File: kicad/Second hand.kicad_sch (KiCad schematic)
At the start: 74 parts, among them Q201 DMN32D2, Q210 DMP2900, Q223 DMN32D2, Q232 DMP2900, Q245 DMN32D2, Q254 DMP2900, Q267 DMN32D2, Q289 DMN32D2, U201 74HC595, U202 74HC595

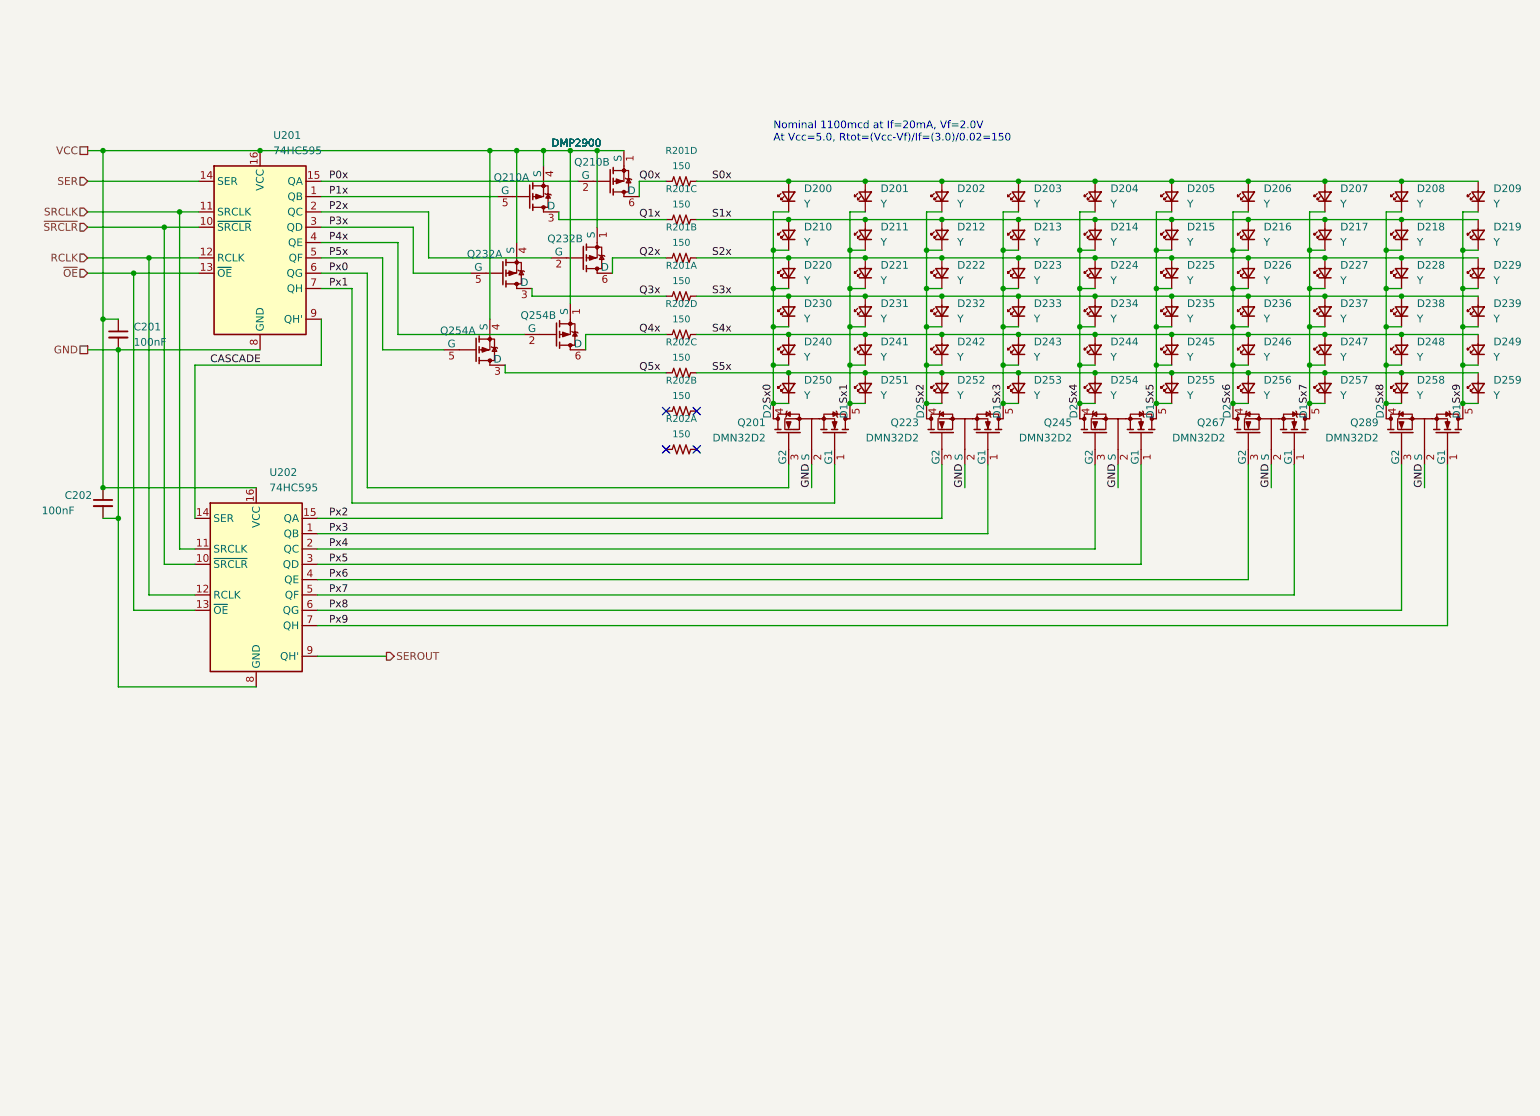
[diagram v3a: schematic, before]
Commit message: Continue wiring MOSFET switches
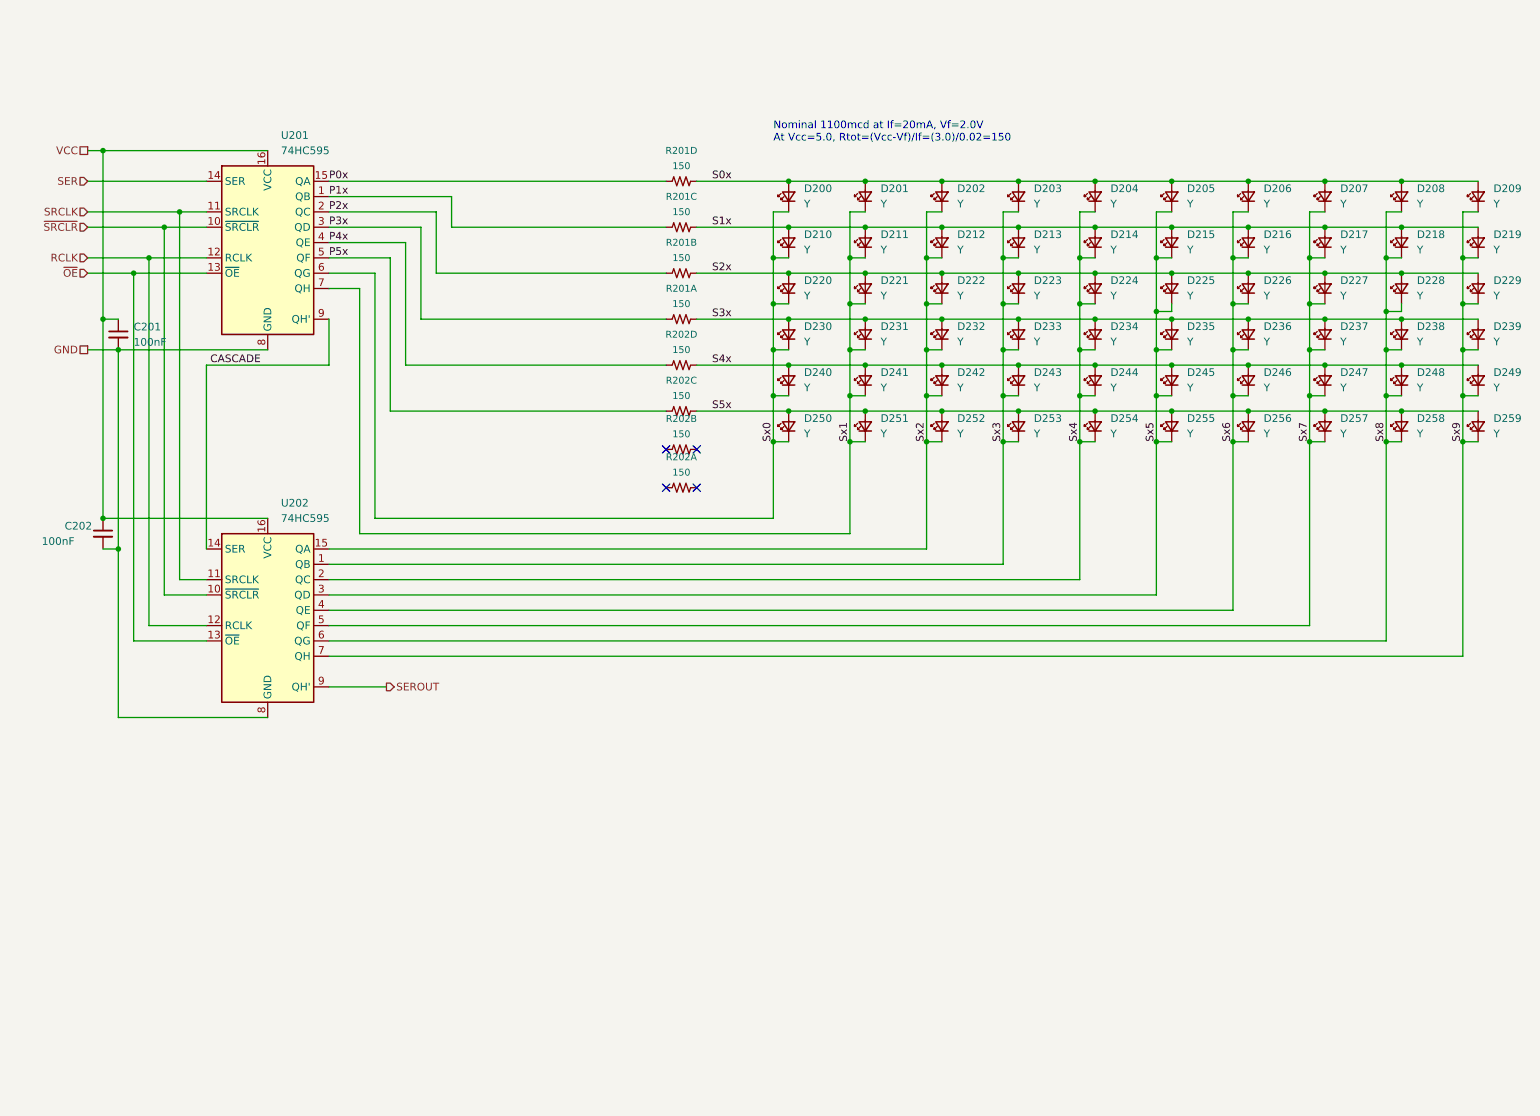
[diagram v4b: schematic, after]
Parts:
- removed Q201, Q223, Q245, Q267, Q289: DMN32D2, Package_TO_SOT_SMD:SOT-353_SC-70-5, symbol KwanSystems:NMOS_DUAL_COMMON_SOURCE
- removed Q210, Q232, Q254: DMP2900, Package_TO_SOT_SMD:SOT-363_SC-70-6, symbol KwanSystems:PMOS_DUAL
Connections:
- net Px0 is gone; now on net Sx0: U201.6 (QG)
- net Px1 is gone; now on net Sx1: U201.7 (QH)
- net Px2 is gone; now on net Sx2: U202.15 (QA)
- net Px3 is gone; now on net Sx3: U202.1 (QB)
- net Px4 is gone; now on net Sx4: U202.2 (QC)
- net Px5 is gone; now on net Sx5: U202.3 (QD)
- net Px6 is gone; now on net Sx6: U202.4 (QE)
- net Px7 is gone; now on net Sx7: U202.5 (QF)
- net Px8 is gone; now on net Sx8: U202.6 (QG)
- net Px9 is gone; now on net Sx9: U202.7 (QH)
- net Q0x is gone; now on net P0x: R201.4
- net Q1x is gone; now on net P1x: R201.3 (4)
- net Q2x is gone; now on net P2x: R201.2 (4)
- net Q3x is gone; now on net P3x: R201.1 (4)
- net Q4x is gone; now on net P4x: R202.4
- net Q5x is gone; now on net P5x: R202.3 (4)
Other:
- moved on the sheet: C202, D210, D211, D212, D213, D214, D215, D216, D217, D218, D219, D220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

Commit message: Matrix8x8 stuff
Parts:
- removed R201, R202: 150, KwanSystems:R_Array_Convex_4x0402, symbol KwanSystems:RP4
- removed U202: 74HC595, Package_SO:TSSOP-16_4.4x5mm_P0.65mm, symbol 74xx:74HC595
- added C1, C2: 100nF, Capacitor_SMD:C_0603_1608Metric, symbol Device:C_Small
- added D0, D1, D10, D11, D12, D13, D14, D15, D16, D17, D18, D19, D2, D20, D21, D22, D23, D24, D25, D26, D27, D28, D29, D3, D30, D31, D32, D33, D34, D35, D36, D37, D38, D39, D4, D40, D41, D42, D43, D44, D45, D46, D47, D48, D49, D5, D50, D51, D52, D53, D54, D55, D56, D57, D58, D59, D6, D7, D8, D9: Y, KwanSystems:D_KINGBRIGHT_DOME, symbol Device:LED_Small
- added Q1, Q2, Q201, Q202, Q203, Q204, Q3, Q4: PMOS_DUAL, Package_TO_SOT_SMD:SOT-363_SC-70-6, symbol KwanSystems:PMOS_DUAL
- added R1, R201: 1k, Resistor_SMD:R_0603_1608Metric, symbol KwanSystems:RESISTOR
- added U1: 74HC595, Package_SO:TSSOP-16_4.4x5mm_P0.65mm, symbol 74xx:74HC595
- added U2, U202: STP08CP05, Package_SO:TSSOP-16_4.4x5mm_P0.65mm, symbol Driver_LED:STP08CP05
- C201, C202: Digikey 445-5613-1-ND -> 445-5666-1-ND; Part Number CGA2B1X7R1C104K050BC -> CGA3E2X7R1H104K080AA
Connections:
- net ~{SRCLR} is gone; now on net VCC: U201.10 (~{SRCLR})
- net CASCADE: now also U202.2 (SDI)
- net GND: now also U201.13 (~{OE}), R201.1, U202.1 (GND)
- net P0x: now also Q201.5 (G)
- net P1x: now also Q201.2 (G)
- net P2x: now also Q202.5 (G)
- net P3x: now also Q202.2 (G)
- net P4x: now also Q203.5 (G)
- net P5x: now also Q203.2 (G)
- net RCLK: now also U202.4 (LE)
- net S0x: now also Q201.3 (D); no longer D208.2 (A), D209.2 (A)
- net S1x: now also D208.2 (A), D209.2 (A), Q201.6 (D); no longer D216.2 (A), D217.2 (A), D218.2 (A), D219.2 (A)
- net S2x: now also D216.2 (A), D217.2 (A), D218.2 (A), D219.2 (A), Q202.3 (D); no longer D224.2 (A), D225.2 (A), D226.2 (A), D227.2 (A), D228.2 (A), D229.2 (A)
- net S3x: now also D224.2 (A), D225.2 (A), D226.2 (A), D227.2 (A), D228.2 (A), D229.2 (A), Q202.6 (D); no longer D232.2 (A), D233.2 (A), D234.2 (A), D235.2 (A), D236.2 (A), D237.2 (A), D238.2 (A), D239.2 (A)
- net S4x: now also D232.2 (A), D233.2 (A), D234.2 (A), D235.2 (A), D236.2 (A), D237.2 (A), D238.2 (A), D239.2 (A), Q203.3 (D); no longer D240.2 (A), D241.2 (A), D242.2 (A), D243.2 (A), D244.2 (A), D245.2 (A), D246.2 (A), D247.2 (A), D248.2 (A), D249.2 (A)
- net S5x: now also D240.2 (A), D241.2 (A), D242.2 (A), D243.2 (A), D244.2 (A), D245.2 (A), D246.2 (A), D247.2 (A), Q203.6 (D); no longer D250.2 (A), D251.2 (A), D252.2 (A), D253.2 (A), D254.2 (A), D255.2 (A), D256.2 (A), D257.2 (A), D258.2 (A), D259.2 (A)
- net SEROUT: now also U202.14 (SDO)
- net SRCLK: now also U202.3 (CLK)
- net Sx0: now also D208.1 (K), D216.1 (K), D224.1 (K), D232.1 (K), D248.1 (K), D256.1 (K), U202.5 (OUT0); no longer D210.1 (K), D220.1 (K), D230.1 (K), D250.1 (K), U201.6 (QG)
- net Sx1: now also D209.1 (K), D217.1 (K), D225.1 (K), D233.1 (K), D249.1 (K), D257.1 (K), U202.6 (OUT1); no longer D211.1 (K), D221.1 (K), D231.1 (K), D251.1 (K), U201.7 (QH)
- net Sx2: now also D210.1 (K), D218.1 (K), D226.1 (K), D234.1 (K), D250.1 (K), D258.1 (K), U202.7 (OUT2); no longer D212.1 (K), D222.1 (K), D232.1 (K), D252.1 (K)
- net Sx3: now also D211.1 (K), D219.1 (K), D227.1 (K), D235.1 (K), D251.1 (K), D259.1 (K), U202.8 (OUT3); no longer D213.1 (K), D223.1 (K), D233.1 (K), D253.1 (K)
- net Sx4: now also D212.1 (K), D220.1 (K), D228.1 (K), D236.1 (K), D252.1 (K), U202.9 (OUT4); no longer D214.1 (K), D224.1 (K), D234.1 (K), D254.1 (K)
- net Sx5: now also D213.1 (K), D221.1 (K), D229.1 (K), D237.1 (K), D253.1 (K), U202.10 (OUT5); no longer D215.1 (K), D225.1 (K), D235.1 (K), D255.1 (K)
- net Sx6: now also D214.1 (K), D222.1 (K), D230.1 (K), D238.1 (K), D254.1 (K), U202.11 (OUT6); no longer D216.1 (K), D226.1 (K), D236.1 (K), D256.1 (K)
- net Sx7: now also D215.1 (K), D223.1 (K), D231.1 (K), D239.1 (K), D255.1 (K), U202.12 (OUT7); no longer D217.1 (K), D227.1 (K), D237.1 (K), D257.1 (K)
- net VCC: now also Q201.1 (S), Q201.4 (S), Q202.1 (S), Q202.4 (S), Q203.1 (S), Q203.4 (S), Q204.1 (S), Q204.4 (S), U202.16 (VDD)
- net ~{OE}: now also U202.13 (~{OE}); no longer U201.13 (~{OE})
- removed net Sx8: D208.1 (K), D218.1 (K), D228.1 (K), D238.1 (K), D248.1 (K), D258.1 (K)
- removed net Sx9: D209.1 (K), D219.1 (K), D229.1 (K), D239.1 (K), D249.1 (K), D259.1 (K)
- new net P6x: Q204.5 (G), U201.6 (QG)
- new net P7x: Q204.2 (G), U201.7 (QH)
- new net R_EXT: R201.2, U202.15 (R-EXT)
- new net S6x: D248.2 (A), D249.2 (A), D250.2 (A), D251.2 (A), D252.2 (A), D253.2 (A), D254.2 (A), D255.2 (A), Q204.3 (D)
- new net S7x: D256.2 (A), D257.2 (A), D258.2 (A), D259.2 (A), Q204.6 (D)
- no-connect marks 4 -> 182
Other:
- note added: "Rext (R) Iout (mA) 6740 3 3930 5 1913 10 963 20 386 50 241 80 124 130"
- note removed: "Nominal 1100mcd at If=20mA, Vf=2.0V At Vcc=5.0, Rtot=(Vcc-Vf)/If=(3.0)/0.02=150"
